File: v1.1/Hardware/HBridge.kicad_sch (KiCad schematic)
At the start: 61 parts, among them J3 TRANSDUCER, Q1 IXXH80N65B4H1, Q2 IXXH80N65B4H1, Q3 IXXH80N65B4H1, Q4 IXXH80N65B4H1, T1 Transformer_1P_1S, U10 HCPL-3120, U11 HCPL-3120, U8 HCPL-3120, U9 HCPL-3120

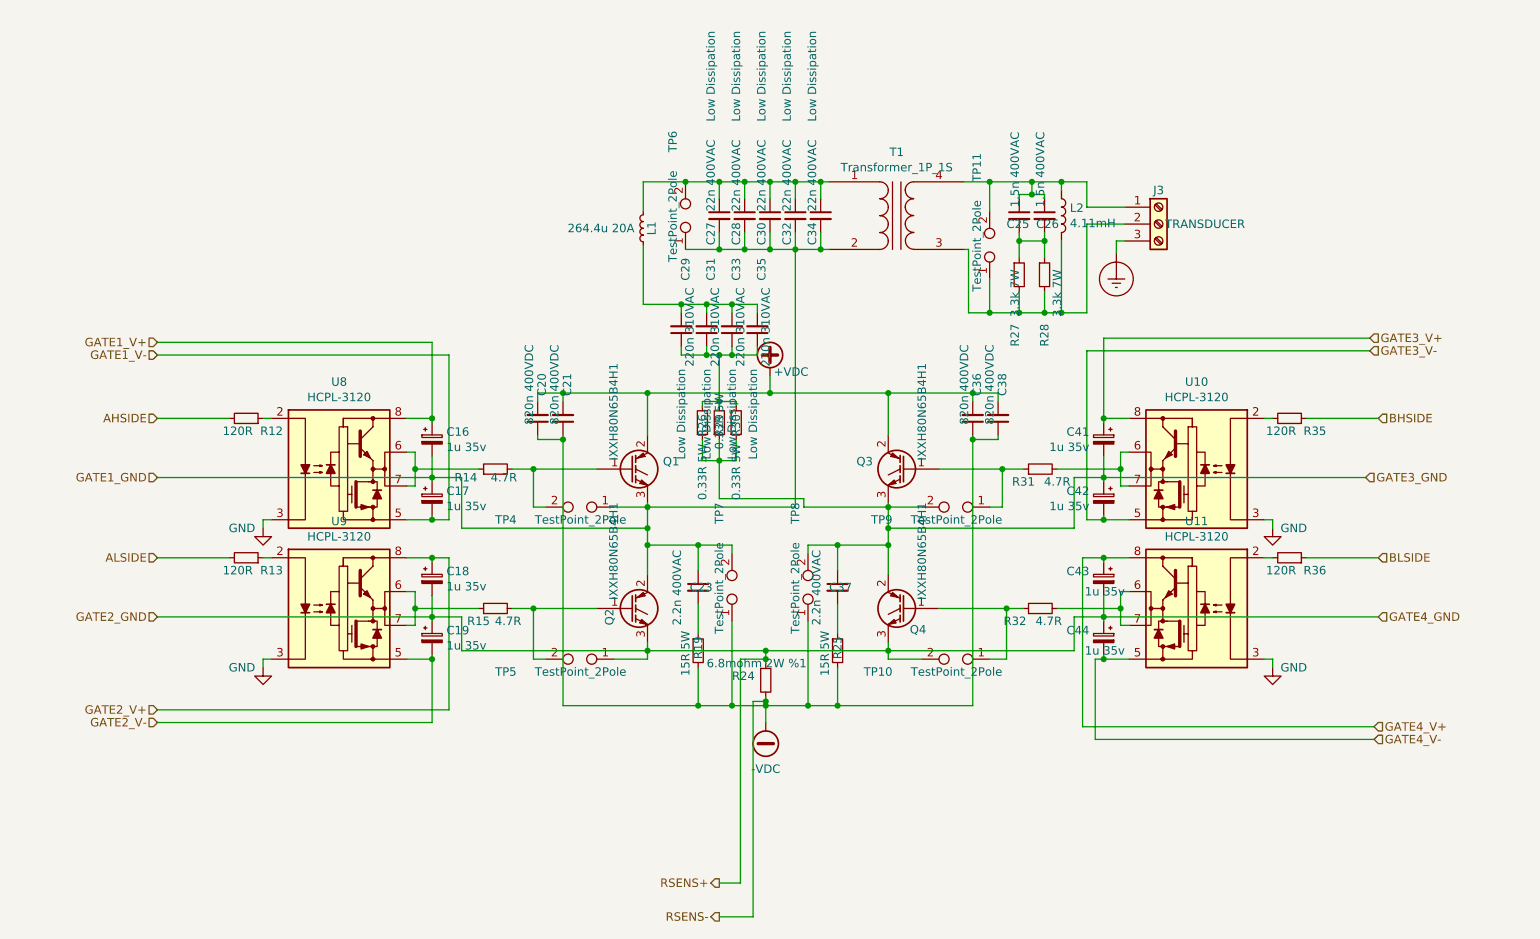
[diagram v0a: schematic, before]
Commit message: v1.1&v1.2 PCB addition.
#####v1.1#####
+Change of MCU; STM32F334C8T6 instead of STM32F103C8T6.
+Filtering 3rd order components of the square wave.
+Use  4 capacitors.
+Adapted to generic transformer(primary 6.4mH, secondary 14.4mH)
+Faster IGBT.

########v1.2#######
+Measures only PZT current and voltage.
+Differential inputs.
+Analog circuitry is capable of measuring four quadrant voltage, current and complex impedance.
+Half bridge configuration.
+Gate resistance of the IGBT's lowered.
+Only USART based touch panel can be connected; not conventional LCD.
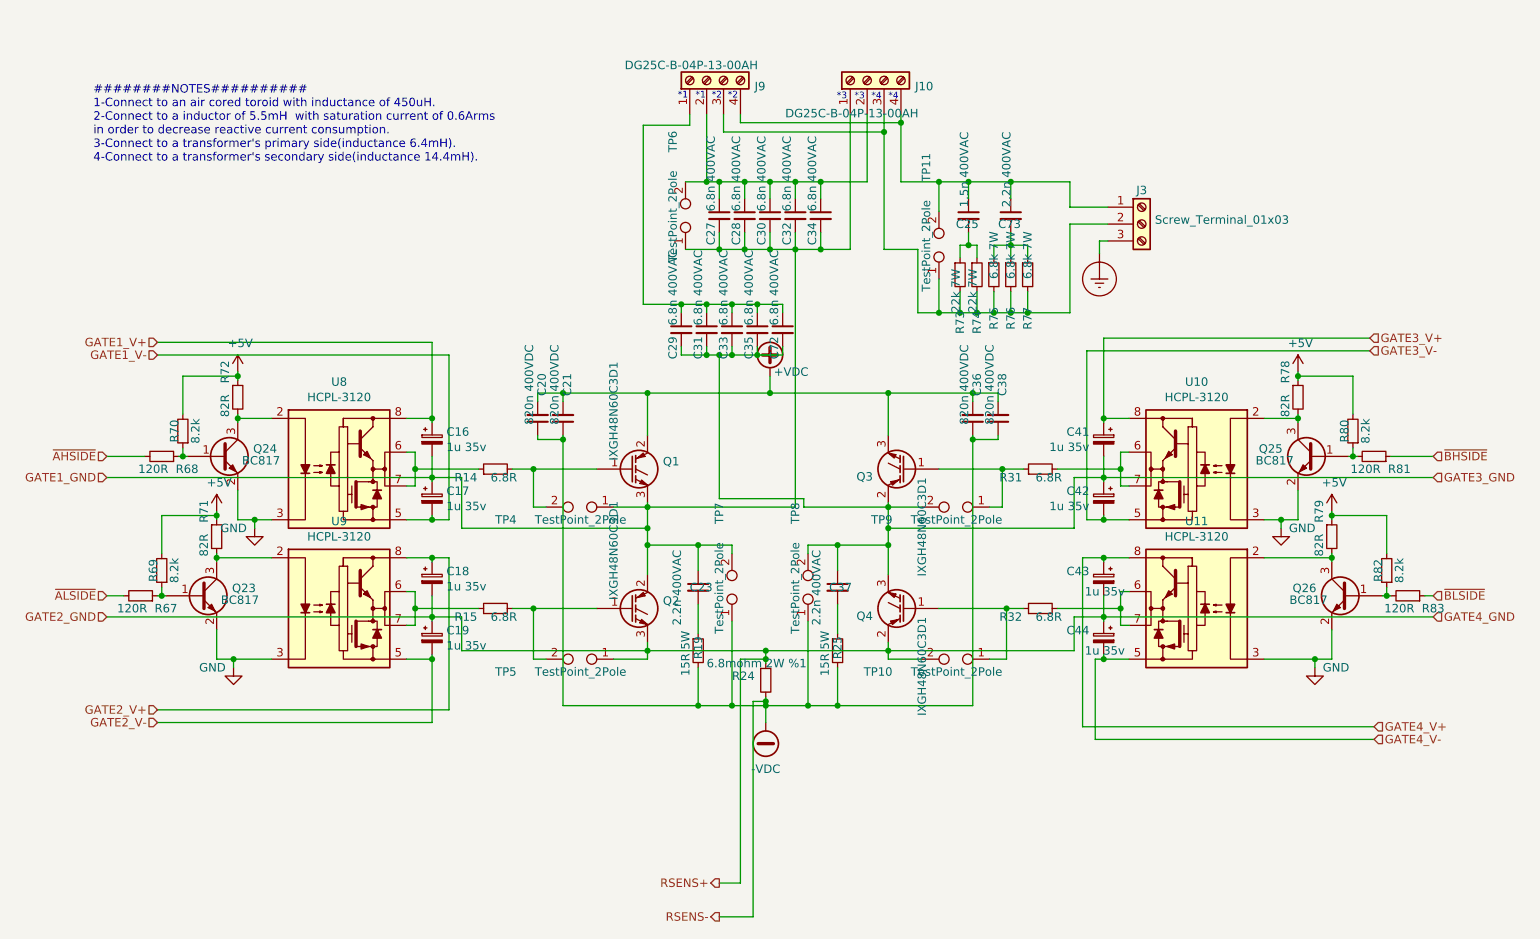
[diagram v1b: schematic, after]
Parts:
- removed C26: 1.5n 400VAC, Capacitor_THT:C_Rect_L18.0mm_W5.0mm_P15.00mm_FKS3_FKP3, symbol Device:C_Small
- removed L1: 264.4u 20A, oe_inductor:Toroid_21mm_38mm, symbol Device:L_Small
- removed L2: 4.11mH, oe_inductor:Toroid_21mm_38mm, symbol Device:L
- removed R12, R13, R35, R36: 120R, Resistor_THT:R_Axial_DIN0207_L6.3mm_D2.5mm_P10.16mm_Horizontal, symbol Device:R_Small
- removed R26, R29, R30: 0.33R 5W, Resistor_THT:R_Axial_Power_L25.0mm_W9.0mm_P30.48mm, symbol Device:R_Small
- removed R28: 3.3k 7W, Resistor_THT:R_Axial_Power_L25.0mm_W9.0mm_P30.48mm, symbol Device:R_Small
- removed T1: Transformer_1P_1S, oe_transformer:Toroid_2x2_26mm_55mm, symbol Device:Transformer_1P_1S
- added C72: 6.8n 400VAC, Capacitor_THT:C_Rect_L18.0mm_W5.0mm_P15.00mm_FKS3_FKP3, symbol Device:C_Small
- added C73: 2.2n 400VAC, Capacitor_THT:C_Rect_L13.0mm_W4.0mm_P10.00mm_FKS3_FKP3_MKS4, symbol Device:C_Small
- added J10, J9: DG25C-B-04P-13-00AH, oe_connector:DG25C-B-04P-13-00AH, symbol Connector:Screw_Terminal_01x04
- added Q23, Q24, Q25, Q26: BC817, Package_TO_SOT_SMD:SOT-23, symbol Transistor_BJT:BC817
- added R67, R68, R81, R83: 120R, Resistor_SMD:R_0805_2012Metric, symbol Device:R_Small
- added R69, R70, R80, R82: 8.2k, Resistor_SMD:R_0805_2012Metric, symbol Device:R_Small
- added R71, R72, R78, R79: 82R, Resistor_SMD:R_0805_2012Metric, symbol Device:R_Small
- added R74: 22k 7W, Resistor_THT:R_Axial_DIN0922_L20.0mm_D9.0mm_P30.48mm_Horizontal, symbol Device:R_Small
- added R75, R76, R77: 6.8k 7W, Resistor_THT:R_Axial_Power_L25.0mm_W9.0mm_P30.48mm, symbol Device:R_Small
- C27, C28, C30, C32, C34: value 22n 400VAC -> 6.8n 400VAC; Link https://www.ozdisan.com/passive-components/capacitors/film-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 -> https://ozdisan.com/passive-components/capacitors/film-capa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; Price 0.56281TL -> 0.74893TL; Properties Low Dissipation -> (none)
- C29, C31, C33, C35: value 220n 310VAC -> 6.8n 400VAC; footprint Capacitor_THT:C_Rect_L18.0mm_W8.0mm_P15.00mm_FKS3_FKP3 -> Capacitor_THT:C_Rect_L18.0mm_W5.0mm_P15.00mm_FKS3_FKP3; Link https://ozdisan.com/passive-components/capacitors/film-capacitors/R463I3220DQM2K -> https://ozdisan.com/passive-components/capacitors/film-capacitors/C323C682J60A605; Price 0.91706TL -> 0.74893TL; Properties Low Dissipation -> (none)
- J3: value TRANSDUCER -> Screw_Terminal_01x03
- Q1, Q2, Q3, Q4: value IXXH80N65B4H1 -> IXGH48N60C3D1; Link https://ozdisan.com/power-semiconductors/igbts/discrete-igb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 -> https://www.ozdisan.com/power-semiconductors/igbts/discrete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; Price 31.66492TL -> 25.41445TL
- R14, R15, R31, R32: value 4.7R -> 6.8R; Link https://ozdisan.com/passive-components/resistors/tht-through-hole-resistors/CFR0W4J047JA50 -> https://ozdisan.com/passive-components/resistors/tht-through-hole-resistors/CFR0W4J068JA50; Price 0.04762TL -> 0.04819TL
- R73: renamed from R27; value 3.3k 7W -> 22k 7W; footprint Resistor_THT:R_Axial_Power_L25.0mm_W9.0mm_P30.48mm -> Resistor_THT:R_Axial_DIN0922_L20.0mm_D9.0mm_P30.48mm_Horizontal; Link https://ozdisan.com/passive-components/resistors/tht-through-hole-resistors/MOR07SJ0332B00 -> https://ozdisan.com/passive-components/resistors/tht-through-hole-resistors/MOR07SJ0223B00; Price 1.35143TL -> 1.35215TL
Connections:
- net +VDC: now also Q3.3 (E); no longer Q3.2 (C)
- net GATE1_GND: now also J10.1 (Pin_1)
- net GATE2_GND: now also Q4.2 (C); no longer Q4.3 (E)
- net GATE3_GND: now also C29.2, C31.2, C33.2, C35.2, Q3.2 (C), Q4.3 (E), C72.2; no longer Q3.3 (E), Q4.2 (C)
- net GND: now also Q23.2 (E), Q24.2 (E), Q25.2 (E), Q26.2 (E)
- net at C29.1, C31.1, C33.1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: now also C72.1, J9.1 (Pin_1)
- net at U9.2 (A): now also Q23.3 (C), R71.2
- net at U8.2 (A): now also Q24.3 (C), R72.2
- net at C25.2, R73.1: now also R74.1
- net at J3.2 (Pin_2), R73.2, TP11.1: now also J10.3 (Pin_3), J9.3 (Pin_3), R74.2, R75.2, R76.2, R77.2
- net at C25.1, J3.1 (Pin_1), TP11.2: now also C73.1, J10.4 (Pin_4), J9.4 (Pin_4)
- net at U10.2 (A): now also Q25.3 (C), R78.2
- net at U11.2 (A): now also Q26.3 (C), R79.2
- net at C27.1, C28.1, C30.1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: now also J10.2 (Pin_2), J9.2 (Pin_2)
- new net: C73.2, R75.1, R76.1, R77.1
- new net: Q24.1 (B), R68.1, R70.1
- new net: Q26.1 (B), R82.1, R83.2
- new net: Q23.1 (B), R67.1, R69.1
- new net: Q25.1 (B), R80.1, R81.2
- new net +5V: R69.2, R70.2, R71.1, R72.1, R78.1, R79.1, R80.2, R82.2
- new net ~AHSIDE: R68.2
- new net ~ALSIDE: R67.2
- new net ~BHSIDE: R81.1
- new net ~BLSIDE: R83.1
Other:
- note added: "########NOTES########## 1-Connect to an air cored toroid with inductance of 450uH. 2-Connect to a inductor of 5.5mH with saturation current of 0.6Arms in order to decrease reactive current consumption. 3-Connect to a transformer's primary side(inductance 6.4mH). 4-Connect to a transformer's secondary side(inductance 14.4mH)."
- note added: "*1"
- note added: "*2"
- note added: "*3"
- note added: "*4"
- moved on the sheet: C25, J3, R73, TP11
